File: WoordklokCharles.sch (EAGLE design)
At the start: 33 parts, among them IC1 74HC595N, IC2 74HC595N, IC3 78L33, IC4 MCP1702-5002, Q1 16MHz, U1 ATMEGA328P, X2 22-23-2021

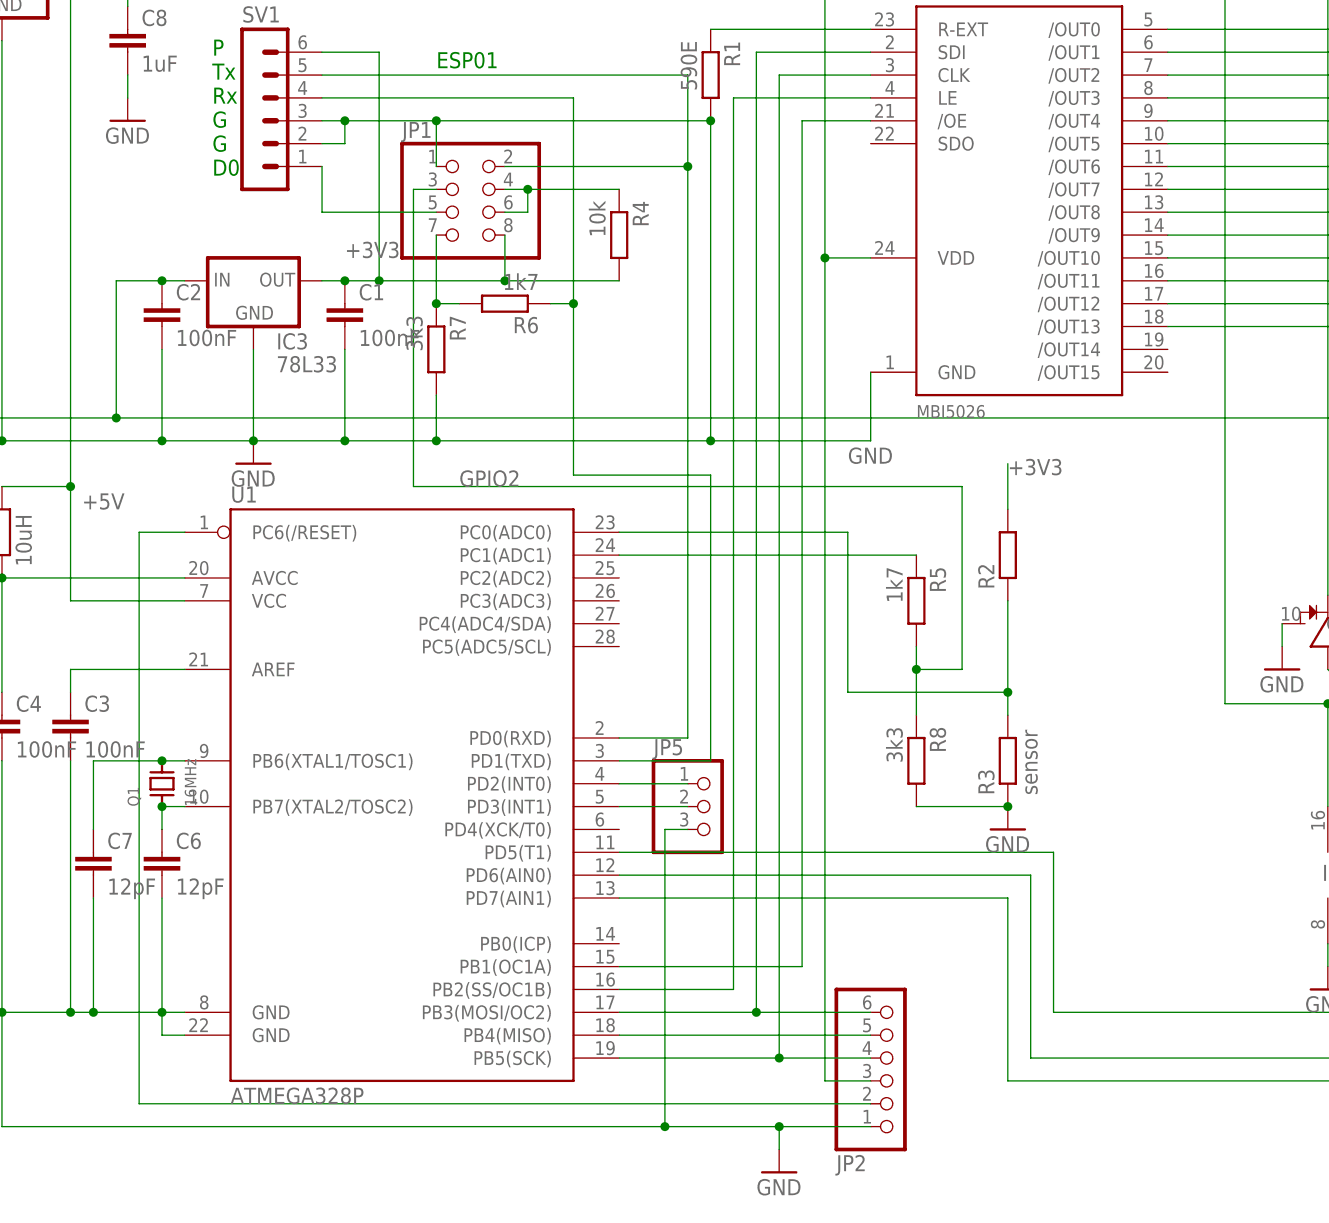
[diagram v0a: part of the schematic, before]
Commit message: V3.0 of CADsoft Eagle files,
V3.0: changed IC3 to MCP1702-33
V2.0: added pull-up resistors for ESP01, several minor corrections
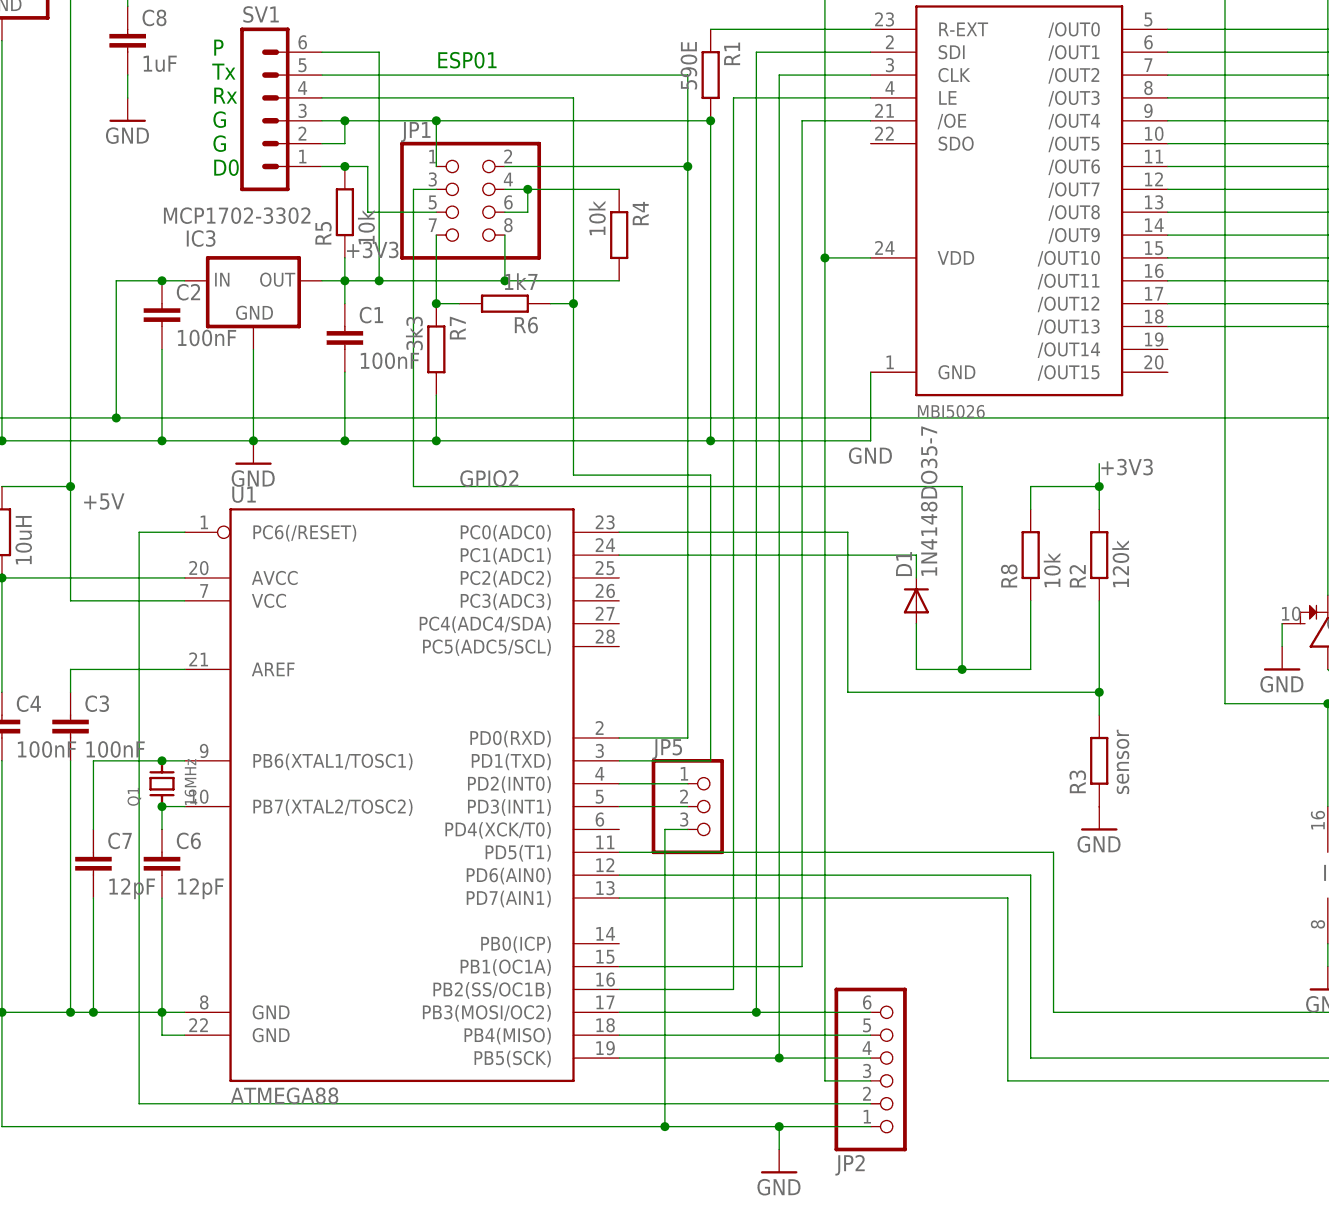
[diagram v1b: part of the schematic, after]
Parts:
- added D1: 1N4148DO35-7, diode:1N4148DO35-7
- IC3: value 78L33 -> MCP1702-3302; device v-reg:78LXX -> adafruit:MCP1700TRI
- R2: value (none) -> 120k
- R5: value 1k7 -> 10k; device rcl:R-EU_0204/7 -> rcl:R-EU_0204/2V
- R8: value 3k3 -> 10k
- U1: value ATMEGA328P -> ATMEGA88
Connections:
- net +3V3: now also R5.1, R8.2
- net GND: no longer R8.2
- net GPIO2: now also D1.A; no longer R5.2
- net N$29: now also R5.2
- net N$65: now also D1.C; no longer R5.1
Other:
- note added: "Change log V2.0: Corrected errors around pullup of two GPIO's of the ESP01 R Replaced by D1 R8 connected to +3V3 Added R5 V3.0 IC3 Replaced 78L33 by MCP1702-33"
- moved on the sheet: C1, R2, R3, R5, R8
